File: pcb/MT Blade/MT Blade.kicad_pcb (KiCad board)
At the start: 2 copper layers, 99.9 x 99.9 mm, 55 parts, among them J8 Conn_01x07_Socket, J9 Conn_01x08

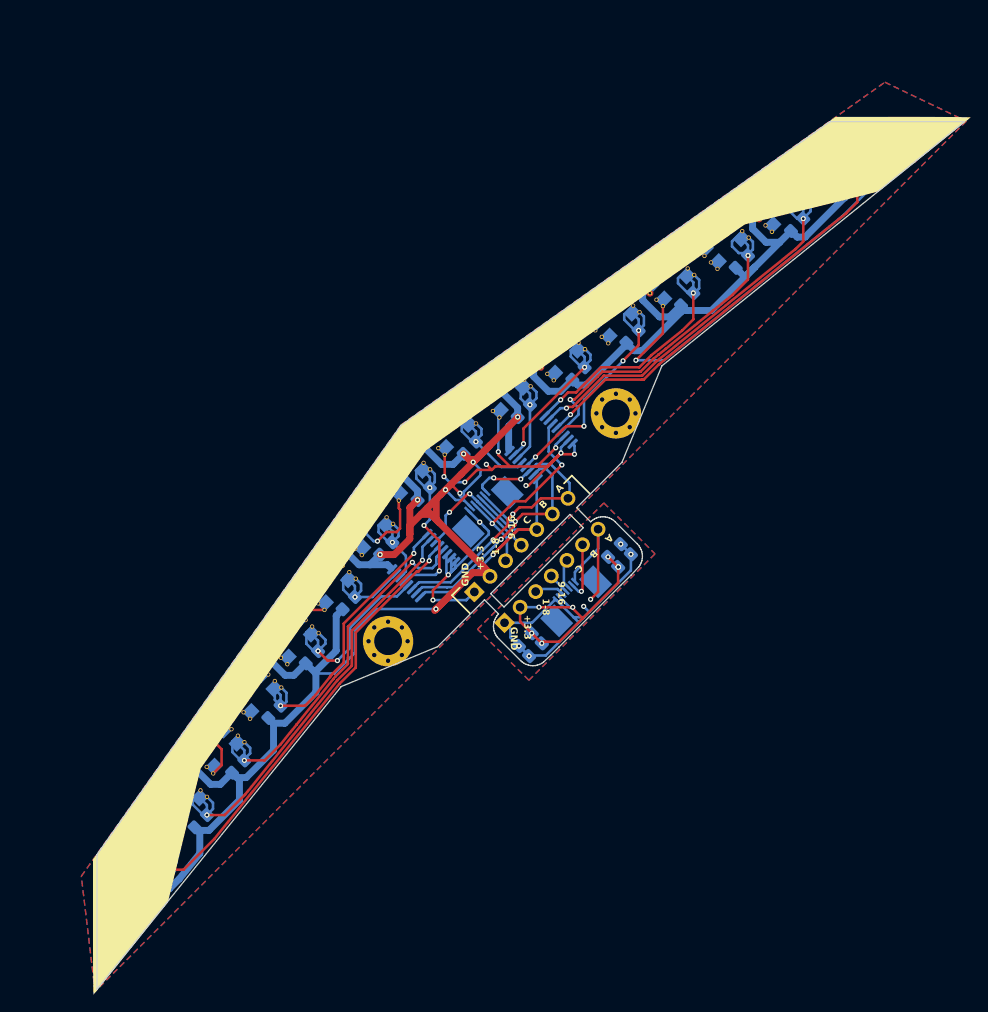
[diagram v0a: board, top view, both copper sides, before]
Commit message: Add lock file for MT Blade PCB design to prevent concurrent edits
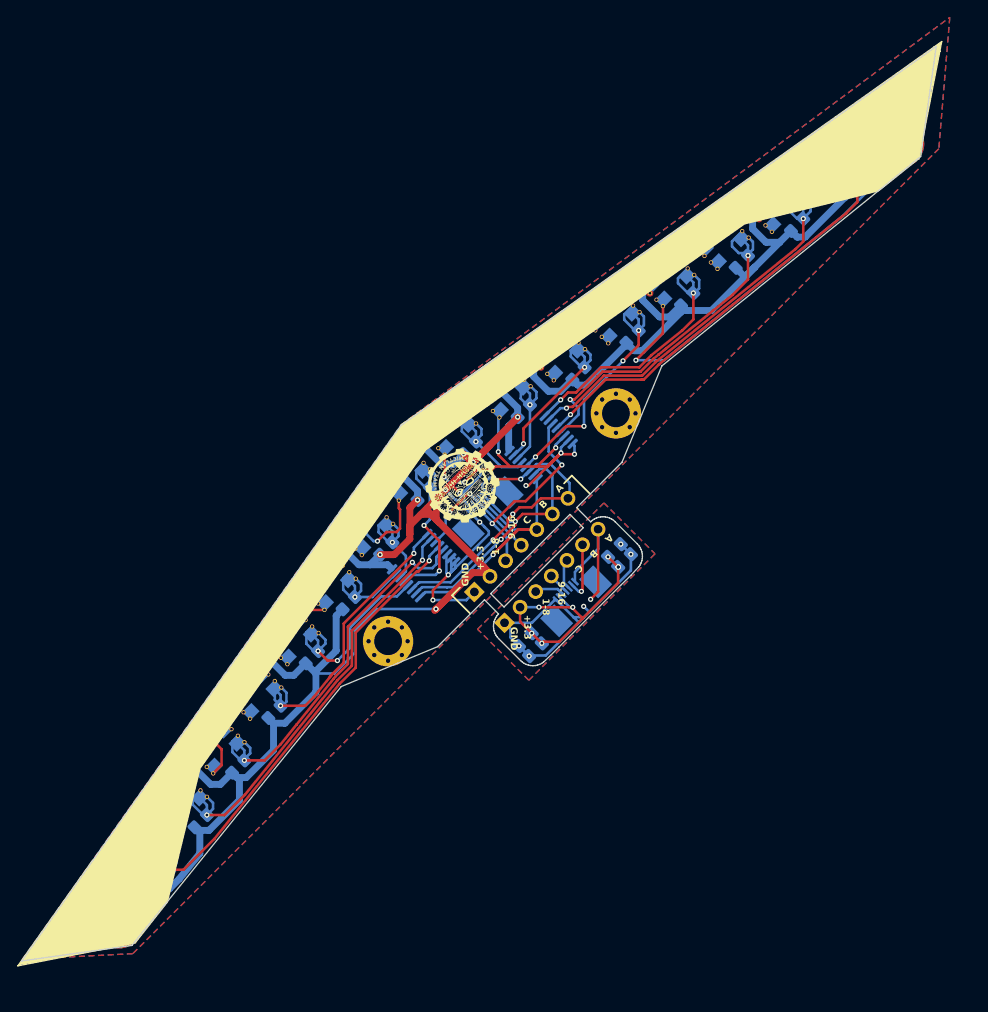
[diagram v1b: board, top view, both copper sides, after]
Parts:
- added G: LOGO, MictlanTeam-Library:MT_Silkscreen 10mm, F.Cu at (150.5, 89.5)
- MUX1, MUX2: footprint custom_footprints:MUX_CD4051B -> MictlanTeam-Library:MUX_CD4051B
- S1, S10, S11, S12, S13, S14, S15, S16, S2, S3, S4, S5, S6, S7, S8, S9: footprint custom_footprints:ITR8307_SMD -> MictlanTeam-Library:ITR8307_SMD
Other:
- board size 99.9 x 99.9 mm -> 105.3 x 105.3 mm
